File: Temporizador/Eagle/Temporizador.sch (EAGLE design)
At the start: 32 parts, among them IC1 7805TV, J1 DCJ0202, Q1 BD139

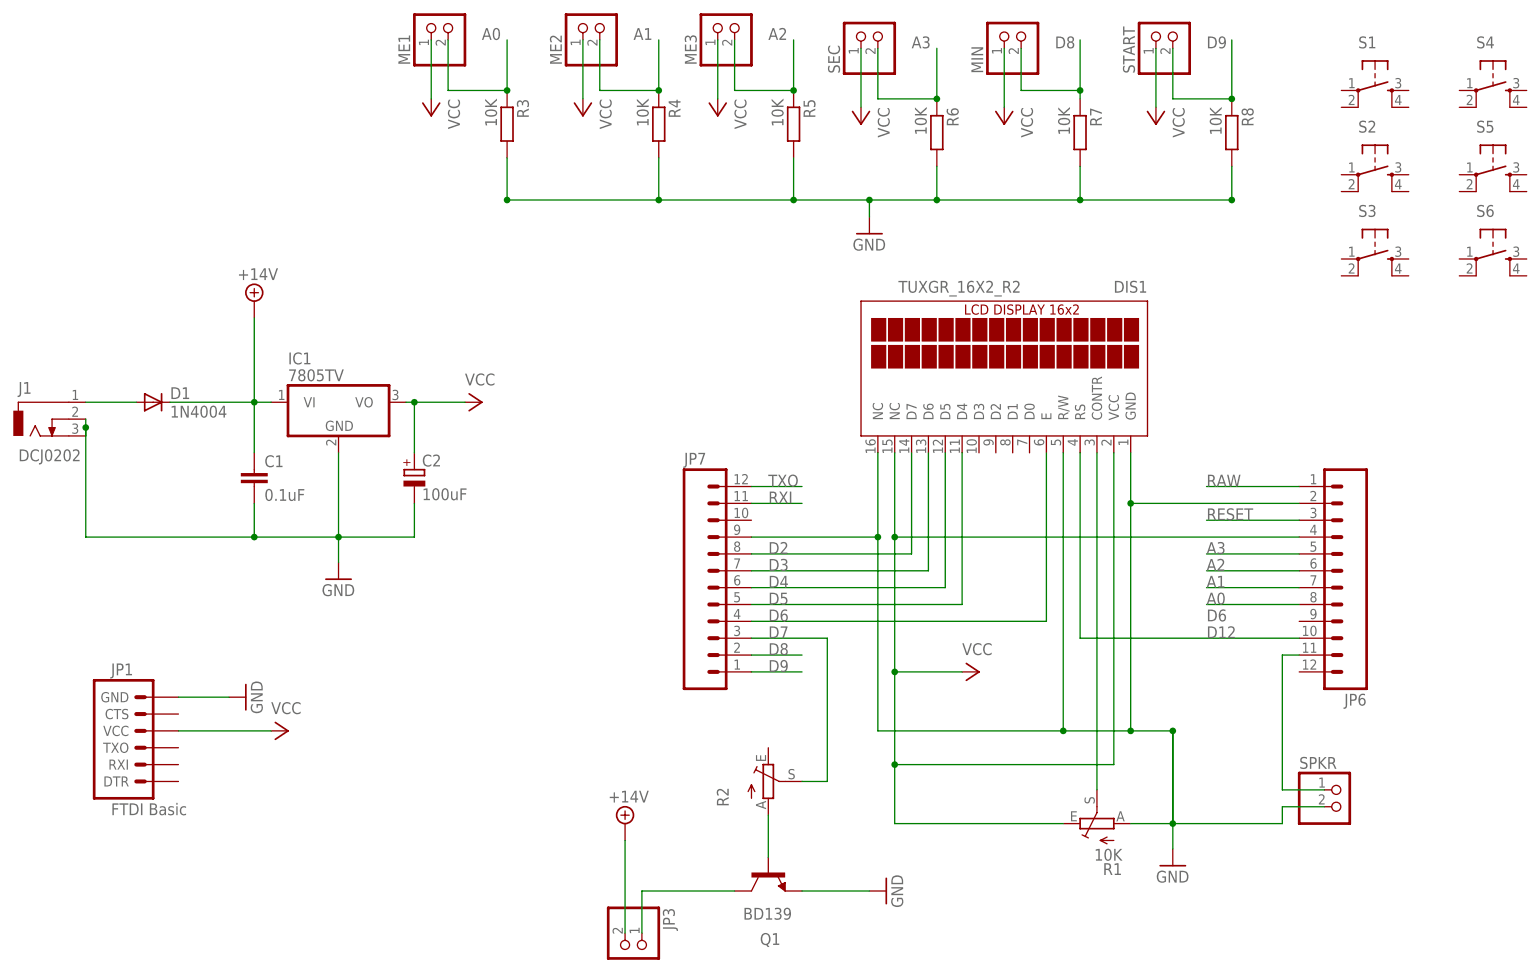
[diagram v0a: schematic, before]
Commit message: Board v1.2
Added more useful pins, comments and larger pads for better soldering
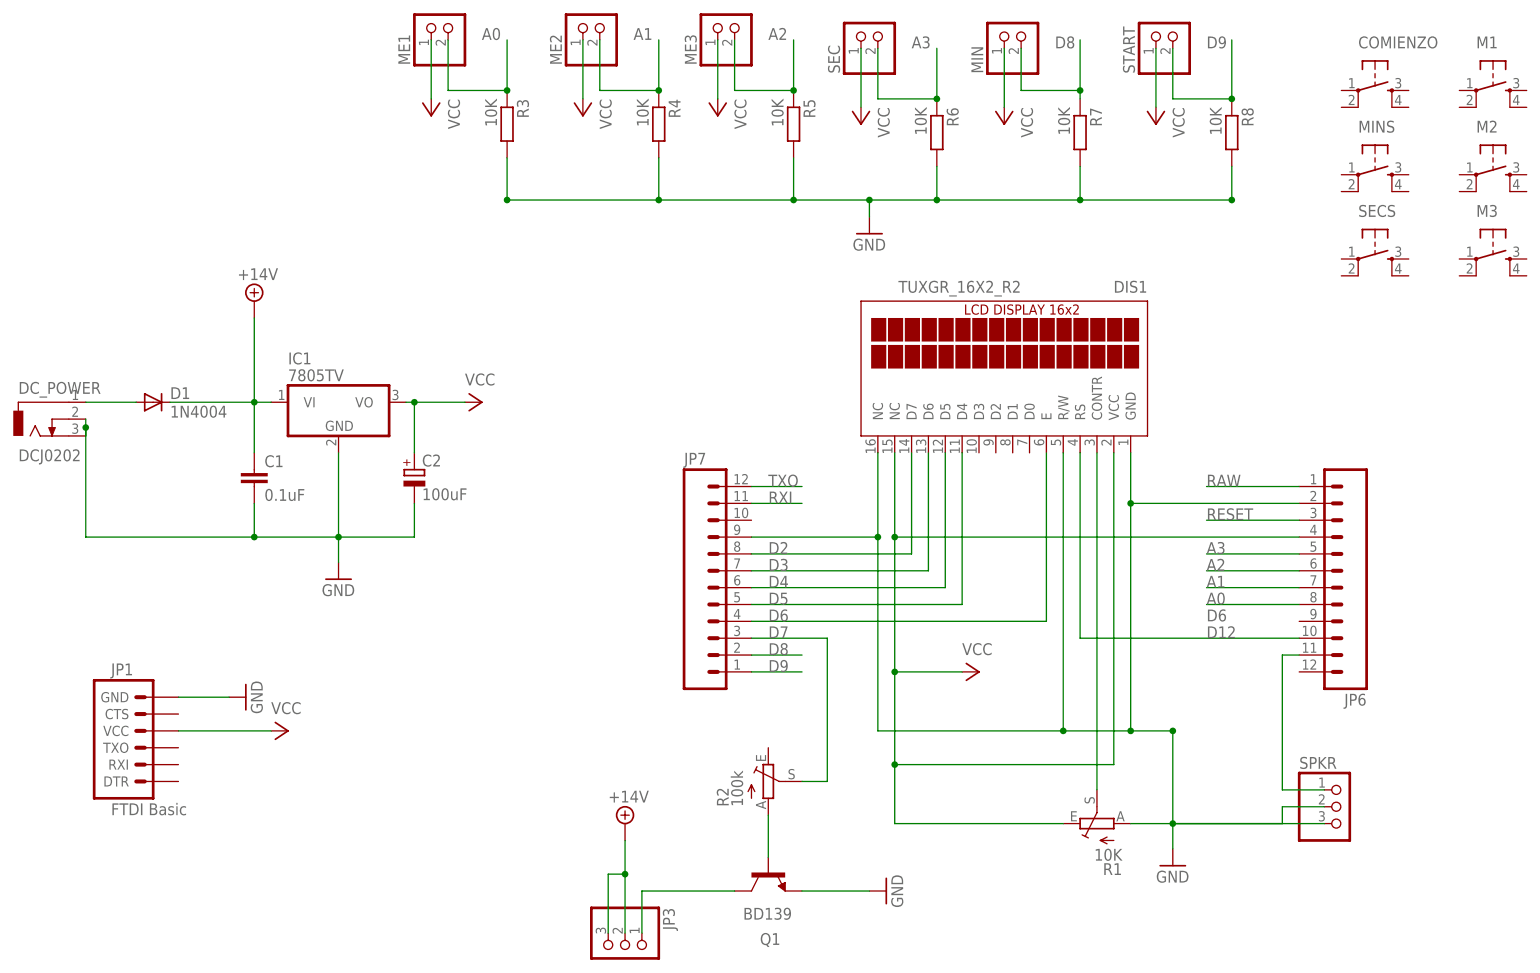
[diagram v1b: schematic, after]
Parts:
- JP3, SPKR: device pinhead:PINHD-1X2 -> pinhead:PINHD-1X3
- JP6, JP7: value M12PTH -> M12LONGPADS; device SparkFun:M12PTH -> SparkFun-Connectors:M12LONGPADS
- R2: value (none) -> 100k
- renumbered J1 to DC_POWER, S1 to COMIENZO, S2 to MINS, S3 to SECS, S4 to M1, S5 to M2, S6 to M3
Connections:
- net +14V: now also JP3.3
- net GND: now also SPKR.3
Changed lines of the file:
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@@
 <layer number="144" name="Drill_legend" color="7" fill="1" visible="no" active="yes"/>
 <layer number="151" name="HeatSink" color="7" fill="1" visible="yes" active="yes"/>
+<layer number="199" name="Contour" color="7" fill="1" visible="yes" active="yes"/>
 <layer number="200" name="200bmp" color="1" fill="10" visible="no" active="no"/>
 <layer number="201" name="201bmp" color="2" fill="1" visible="no" active="no"/>
@@
 </classes>
 <parts>
-<part name="JP6" library="SparkFun" deviceset="M12" device="PTH" value=""/>
-<part name="JP7" library="SparkFun" deviceset="M12" device="PTH" value=""/>
+<part name="JP6" library="SparkFun-Connectors" deviceset="M12" device="LONGPADS" value=""/>
+<part name="JP7" library="SparkFun-Connectors" deviceset="M12" device="LONGPADS" value=""/>
 <part name="JP1" library="SparkFun" deviceset="ARDUINO_SERIAL_PROGRAM" device="PTH" value="FTDI Basic"/>
 <part name="IC1" library="linear" deviceset="78*" device="TV" technology="05"/>
-<part name="J1" library="con-jack" deviceset="DCJ0202" device=""/>
+<part name="DC_POWER" library="con-jack" deviceset="DCJ0202" device=""/>
 <part name="C1" library="rcl" deviceset="C-EU" device="025-030X050" value="0.1uF"/>
 <part name="C2" library="rcl" deviceset="CPOL-EU" device="E2.5-7" value="100uF"/>
@@
 <part name="GND3" library="supply1" deviceset="GND" device=""/>
 <part name="R1" library="pot" deviceset="TRIM_EU-" device="CA6V" value="10K"/>
-<part name="R2" library="pot" deviceset="TRIM_EU-" device="CA6V"/>
+<part name="R2" library="pot" deviceset="TRIM_EU-" device="CA6V" value="100k"/>
 <part name="DIS1" library="display-lcd" deviceset="TUXGR_16X2_R2" device=""/>
 <part name="Q1" library="transistor-npn" deviceset="BD139*" device=""/>
 <part name="P+3" library="supply1" deviceset="VCC" device=""/>
 <part name="GND4" library="supply1" deviceset="GND" device=""/>
-<part name="JP3" library="pinhead" deviceset="PINHD-1X2" device=""/>
+<part name="JP3" library="pinhead" deviceset="PINHD-1X3" device=""/>
 <part name="SUPPLY2" library="supply2" deviceset="+14V" device=""/>
 <part name="D1" library="diode" deviceset="1N4004" device=""/>
@@
 <part name="MIN" library="pinhead" deviceset="PINHD-1X2" device=""/>
 <part name="GND1" library="supply1" deviceset="GND" device=""/>
-<part name="SPKR" library="pinhead" deviceset="PINHD-1X2" device=""/>
-<part name="S1" library="SparkFun-Electromechanical" deviceset="TAC_SWITCH" device="PTH"/>
-<part name="S2" library="SparkFun-Electromechanical" deviceset="TAC_SWITCH" device="PTH"/>
-<part name="S3" library="SparkFun-Electromechanical" deviceset="TAC_SWITCH" device="PTH"/>
-<part name="S4" library="SparkFun-Electromechanical" deviceset="TAC_SWITCH" device="PTH"/>
-<part name="S5" library="SparkFun-Electromechanical" deviceset="TAC_SWITCH" device="PTH"/>
-<part name="S6" library="SparkFun-Electromechanical" deviceset="TAC_SWITCH" device="PTH"/>
+<part name="SPKR" library="pinhead" deviceset="PINHD-1X3" device=""/>
+<part name="COMIENZO" library="SparkFun-Electromechanical" deviceset="TAC_SWITCH" device="PTH"/>
+<part name="MINS" library="SparkFun-Electromechanical" deviceset="TAC_SWITCH" device="PTH"/>
+<part name="SECS" library="SparkFun-Electromechanical" deviceset="TAC_SWITCH" device="PTH"/>
+<part name="M1" library="SparkFun-Electromechanical" deviceset="TAC_SWITCH" device="PTH"/>
+<part name="M2" library="SparkFun-Electromechanical" deviceset="TAC_SWITCH" device="PTH"/>
+<part name="M3" library="SparkFun-Electromechanical" deviceset="TAC_SWITCH" device="PTH"/>
 <part name="GND5" library="supply1" deviceset="GND" device=""/>
 <part name="FRAME1" library="frames" deviceset="A4L-LOC" device=""/>
@@
 <instance part="JP1" gate="G$1" x="25.4" y="66.04"/>
 <instance part="IC1" gate="A1" x="54.61" y="118.11"/>
-<instance part="J1" gate="G$1" x="8.89" y="115.57"/>
+<instance part="DC_POWER" gate="G$1" x="8.89" y="115.57"/>
 <instance part="C1" gate="G$1" x="41.91" y="107.95"/>
 <instance part="C2" gate="G$1" x="66.04" y="107.95"/>
@@
 <instance part="P+3" gate="VCC" x="151.13" y="77.47" rot="R270"/>
 <instance part="GND4" gate="1" x="137.16" y="44.45" rot="R90"/>
-<instance part="JP3" gate="G$1" x="97.79" y="35.56" rot="R270"/>
+<instance part="JP3" gate="A" x="97.79" y="35.56" rot="R270"/>
 <instance part="SUPPLY2" gate="G$1" x="97.79" y="54.61"/>
 <instance part="D1" gate="1" x="26.67" y="118.11"/>
@@
 <instance part="MIN" gate="G$1" x="157.48" y="173.99" rot="R90"/>
 <instance part="GND1" gate="1" x="40.64" y="73.66" rot="R90"/>
-<instance part="SPKR" gate="G$1" x="205.74" y="57.15"/>
-<instance part="S1" gate="S" x="210.82" y="165.1"/>
-<instance part="S2" gate="S" x="210.82" y="152.4"/>
-<instance part="S3" gate="S" x="210.82" y="139.7"/>
-<instance part="S4" gate="S" x="228.6" y="165.1"/>
-<instance part="S5" gate="S" x="228.6" y="152.4"/>
-<instance part="S6" gate="S" x="228.6" y="139.7"/>
+<instance part="SPKR" gate="A" x="205.74" y="57.15"/>
+<instance part="COMIENZO" gate="S" x="210.82" y="165.1"/>
+<instance part="MINS" gate="S" x="210.82" y="152.4"/>
+<instance part="SECS" gate="S" x="210.82" y="139.7"/>
+<instance part="M1" gate="S" x="228.6" y="165.1"/>
+<instance part="M2" gate="S" x="228.6" y="152.4"/>
+<instance part="M3" gate="S" x="228.6" y="139.7"/>
 <instance part="GND5" gate="1" x="134.62" y="143.51"/>
 <instance part="FRAME1" gate="G$1" x="-12.7" y="12.7" smashed="yes">
@@
 </segment>
 </net>
-<net name="GND" class="1">
-<segment>
-<pinref part="J1" gate="G$1" pin="2"/>
+<net name="GND" class="0">
+<segment>
+<pinref part="DC_POWER" gate="G$1" pin="2"/>
 <wire x1="16.51" y1="115.57" x2="16.51" y2="114.3" width="0.1524" layer="91"/>
-<pinref part="J1" gate="G$1" pin="3"/>
+<pinref part="DC_POWER" gate="G$1" pin="3"/>
 <wire x1="16.51" y1="114.3" x2="16.51" y2="113.03" width="0.1524" layer="91"/>
 <pinref part="C1" gate="G$1" pin="2"/>
@@
 <wire x1="173.99" y1="102.87" x2="173.99" y2="68.58" width="0.1524" layer="91"/>
 <wire x1="173.99" y1="68.58" x2="180.34" y2="68.58" width="0.1524" layer="91"/>
-<wire x1="180.34" y1="68.58" x2="180.34" y2="50.8" width="0.1524" layer="91"/>
+<wire x1="180.34" y1="54.61" x2="180.34" y2="50.8" width="0.1524" layer="91"/>
 <wire x1="173.99" y1="68.58" x2="163.83" y2="68.58" width="0.1524" layer="91"/>
 <junction x="173.99" y="68.58"/>
@@
 <wire x1="199.39" y1="102.87" x2="173.99" y2="102.87" width="0.1524" layer="91"/>
 <junction x="173.99" y="102.87"/>
-<pinref part="SPKR" gate="G$1" pin="2"/>
+<pinref part="SPKR" gate="A" pin="2"/>
 <wire x1="196.85" y1="54.61" x2="196.85" y2="57.15" width="0.1524" layer="91"/>
 <wire x1="196.85" y1="57.15" x2="203.2" y2="57.15" width="0.1524" layer="91"/>
+<pinref part="SPKR" gate="A" pin="3"/>
+<wire x1="180.34" y1="54.61" x2="203.2" y2="54.61" width="0.1524" layer="91"/>
 </segment>
 <segment>
@@
 <segment>
 <pinref part="SUPPLY2" gate="G$1" pin="+14V"/>
-<pinref part="JP3" gate="G$1" pin="2"/>
-<wire x1="97.79" y1="52.07" x2="97.79" y2="38.1" width="0.1524" layer="91"/>
+<pinref part="JP3" gate="A" pin="2"/>
+<wire x1="97.79" y1="52.07" x2="97.79" y2="46.99" width="0.1524" layer="91"/>
+<pinref part="JP3" gate="A" pin="3"/>
+<wire x1="97.79" y1="46.99" x2="97.79" y2="38.1" width="0.1524" layer="91"/>
+<wire x1="97.79" y1="46.99" x2="95.25" y2="46.99" width="0.1524" layer="91"/>
+<wire x1="95.25" y1="46.99" x2="95.25" y2="38.1" width="0.1524" layer="91"/>
+<junction x="97.79" y="46.99"/>
 </segment>
 </net>
@@
 <wire x1="199.39" y1="80.01" x2="196.85" y2="80.01" width="0.1524" layer="91"/>
 <wire x1="196.85" y1="80.01" x2="196.85" y2="59.69" width="0.1524" layer="91"/>
-<pinref part="SPKR" gate="G$1" pin="1"/>
+<pinref part="SPKR" gate="A" pin="1"/>
 <wire x1="196.85" y1="59.69" x2="203.2" y2="59.69" width="0.1524" layer="91"/>
 </segment>
@@
 <net name="N$4" class="0">
 <segment>
-<pinref part="JP3" gate="G$1" pin="1"/>
+<pinref part="JP3" gate="A" pin="1"/>
 <wire x1="100.33" y1="38.1" x2="100.33" y2="44.45" width="0.1524" layer="91"/>
 <pinref part="Q1" gate="G$1" pin="C"/>
@@
 <net name="N$5" class="0">
 <segment>
-<pinref part="J1" gate="G$1" pin="1"/>
+<pinref part="DC_POWER" gate="G$1" pin="1"/>
 <pinref part="D1" gate="1" pin="A"/>
 <wire x1="16.51" y1="118.11" x2="24.13" y2="118.11" width="0.1524" layer="91"/>
